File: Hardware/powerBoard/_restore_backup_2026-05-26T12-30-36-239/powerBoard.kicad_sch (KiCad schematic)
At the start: 44 parts, among them J4 DATA, J5 PWR, J6 AUX, Q1 FS8205A, Q2 AO3400A, U2 AMS1117-3.3, U3 DW01A, U4 MT3608, U5 TP4056

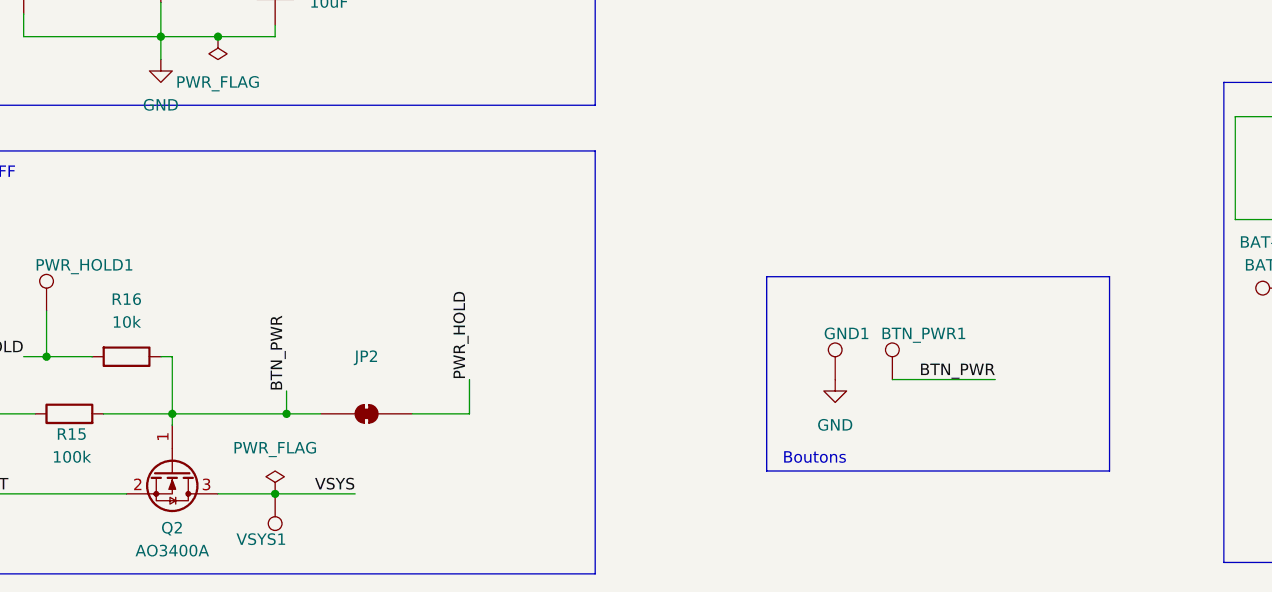
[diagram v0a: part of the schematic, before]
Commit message: refactor: relier le bouton poussoir à l'esp32
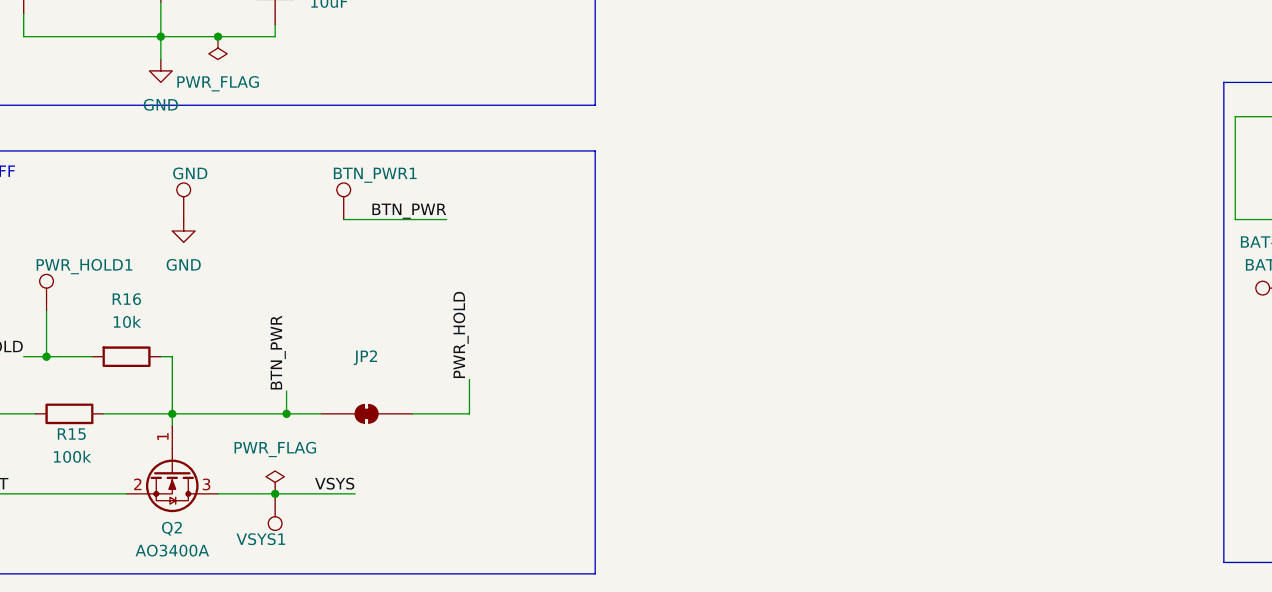
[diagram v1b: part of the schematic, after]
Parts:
- renumbered GND1 to GND
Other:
- note removed: "Boutons"
- moved on the sheet: BTN_PWR1, GND
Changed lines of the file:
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@@
 	)
 	(rectangle
-		(start 111.76 132.08)
-		(end 149.86 153.67)
-		(stroke
-			(width 0)
-			(type default)
-		)
-		(fill
-			(type none)
-		)
-	)
-	(rectangle
-		(start 109.22 132.08)
-		(end 109.22 132.08)
-		(stroke
-			(width 0)
-			(type default)
-		)
-		(fill
-			(type none)
-		)
-	)
-	(rectangle
 		(start 214.63 15.24)
 		(end 257.81 74.93)
@@
 		)
 	)
-	(text "Boutons"
-		(exclude_from_sim no)
-		(at 117.094 152.4 0)
-		(effects
-			(font
-				(size 1.27 1.27)
-			)
-		)
-	)
 	(junction
 		(at 210.82 133.35)
@@
 	(wire
 		(pts
-			(xy 125.73 143.51) (xy 137.16 143.51)
+			(xy 64.77 125.73) (xy 76.2 125.73)
 		)
 		(stroke
@@
 	)
 	(label "BTN_PWR"
-		(at 137.16 143.51 180)
+		(at 76.2 125.73 180)
 		(effects
 			(font
@@
 	(symbol
 		(lib_id "Connector:TestPoint")
-		(at 125.73 143.51 0)
+		(at 64.77 125.73 0)
 		(unit 1)
 		(body_style 1)
@@
 		(dnp no)
 		(property "Reference" "BTN_PWR1"
-			(at 124.46 138.43 0)
+			(at 63.5 120.65 0)
 			(show_name no)
 			(do_not_autoplace no)
@@
 		)
 		(property "Value" ""
-			(at 128.27 141.4779 0)
+			(at 67.31 123.6979 0)
 			(show_name no)
 			(do_not_autoplace no)
@@
 		)
 		(property "Footprint" "TestPoint:TestPoint_Pad_4.0x4.0mm"
-			(at 130.81 143.51 0)
+			(at 69.85 125.73 0)
 			(hide yes)
 			(show_name no)
@@
 		)
 		(property "Datasheet" ""
-			(at 130.81 143.51 0)
+			(at 69.85 125.73 0)
 			(hide yes)
 			(show_name no)
@@
 		)
 		(property "Description" "test point"
-			(at 125.73 143.51 0)
+			(at 64.77 125.73 0)
 			(hide yes)
 			(show_name no)
@@
 	(symbol
 		(lib_id "Connector:TestPoint")
-		(at 119.38 143.51 0)
+		(at 46.99 125.73 0)
 		(unit 1)
 		(body_style 1)
@@
 		(in_pos_files yes)
 		(dnp no)
-		(property "Reference" "GND1"
-			(at 118.11 138.43 0)
+		(property "Reference" "GND"
+			(at 45.72 120.65 0)
 			(show_name no)
 			(do_not_autoplace no)
@@
 		)
 		(property "Value" ""
-			(at 121.92 141.4779 0)
+			(at 49.53 123.6979 0)
 			(show_name no)
 			(do_not_autoplace no)
@@
 		)
 		(property "Footprint" "TestPoint:TestPoint_Pad_4.0x4.0mm"
-			(at 124.46 143.51 0)
+			(at 52.07 125.73 0)
 			(hide yes)
 			(show_name no)
@@
 		)
 		(property "Datasheet" ""
-			(at 124.46 143.51 0)
+			(at 52.07 125.73 0)
 			(hide yes)
 			(show_name no)
@@
 		)
 		(property "Description" "test point"
-			(at 119.38 143.51 0)
+			(at 46.99 125.73 0)
 			(hide yes)
 			(show_name no)
@@
 			(project "powerBoard"
 				(path "/ef9a6e1c-7dcb-475c-bb8f-502c132c52b8"
-					(reference "GND1")
+					(reference "GND")
 					(unit 1)
 				)
@@
 	(symbol
 		(lib_id "power:GND")
-		(at 119.38 143.51 0)
+		(at 46.99 125.73 0)
 		(unit 1)
 		(body_style 1)
@@
 		(fields_autoplaced yes)
 		(property "Reference" "#PWR011"
-			(at 119.38 149.86 0)
+			(at 46.99 132.08 0)
 			(hide yes)
 			(show_name no)
@@
 		)
 		(property "Value" "GND"
-			(at 119.38 148.59 0)
+			(at 46.99 130.81 0)
 			(show_name no)
 			(do_not_autoplace no)
@@
 		)
 		(property "Footprint" ""
-			(at 119.38 143.51 0)
+			(at 46.99 125.73 0)
 			(hide yes)
 			(show_name no)
@@
 		)
 		(property "Datasheet" ""
-			(at 119.38 143.51 0)
+			(at 46.99 125.73 0)
 			(hide yes)
 			(show_name no)
@@
 		)
 		(property "Description" "Power symbol creates a global label with name \"GND\" , ground"
-			(at 119.38 143.51 0)
+			(at 46.99 125.73 0)
 			(hide yes)
 			(show_name no)
